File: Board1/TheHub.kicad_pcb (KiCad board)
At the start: 2 copper layers, 195.6 x 195.6 mm, 56 parts, among them J1 ARM_ADC_1, J10 SCIENCE + WHEELS POWER CONN, J11 RFD900, J12 I2C_1 Test Point, J13 I2C_2 Test Point, J14 ARDUINO NANO LEFT, J15 GPIO Test, J16 I2C_3 Test Point, J17 12V OUT, J18 7.4V IN, J19 ANALOG SENSORS, J2 ARM_ADC_2, J20 GPS, J21 COMPASS, J22 ARDUINO NANO RIGHT, J23 NucleoRight, J3 ARM_PWM_OUT, J4 ARM POWER CONN, J5 NucleoLeft, J6 SCI_ADC_1, J7 SCIENCE_PWM_OUT, J8 12V MAIN POWER, J9 WHEEL_ADC_1, U1 PRE-PCA9685, U2 PRE-ADS1115, U3 PRE-ADS1115, U4 PRE-PCA9685, U5 PRE-ADS1115, U6 TL1963, U7 LM340MP-5.0, U9 PRE-ADS1115

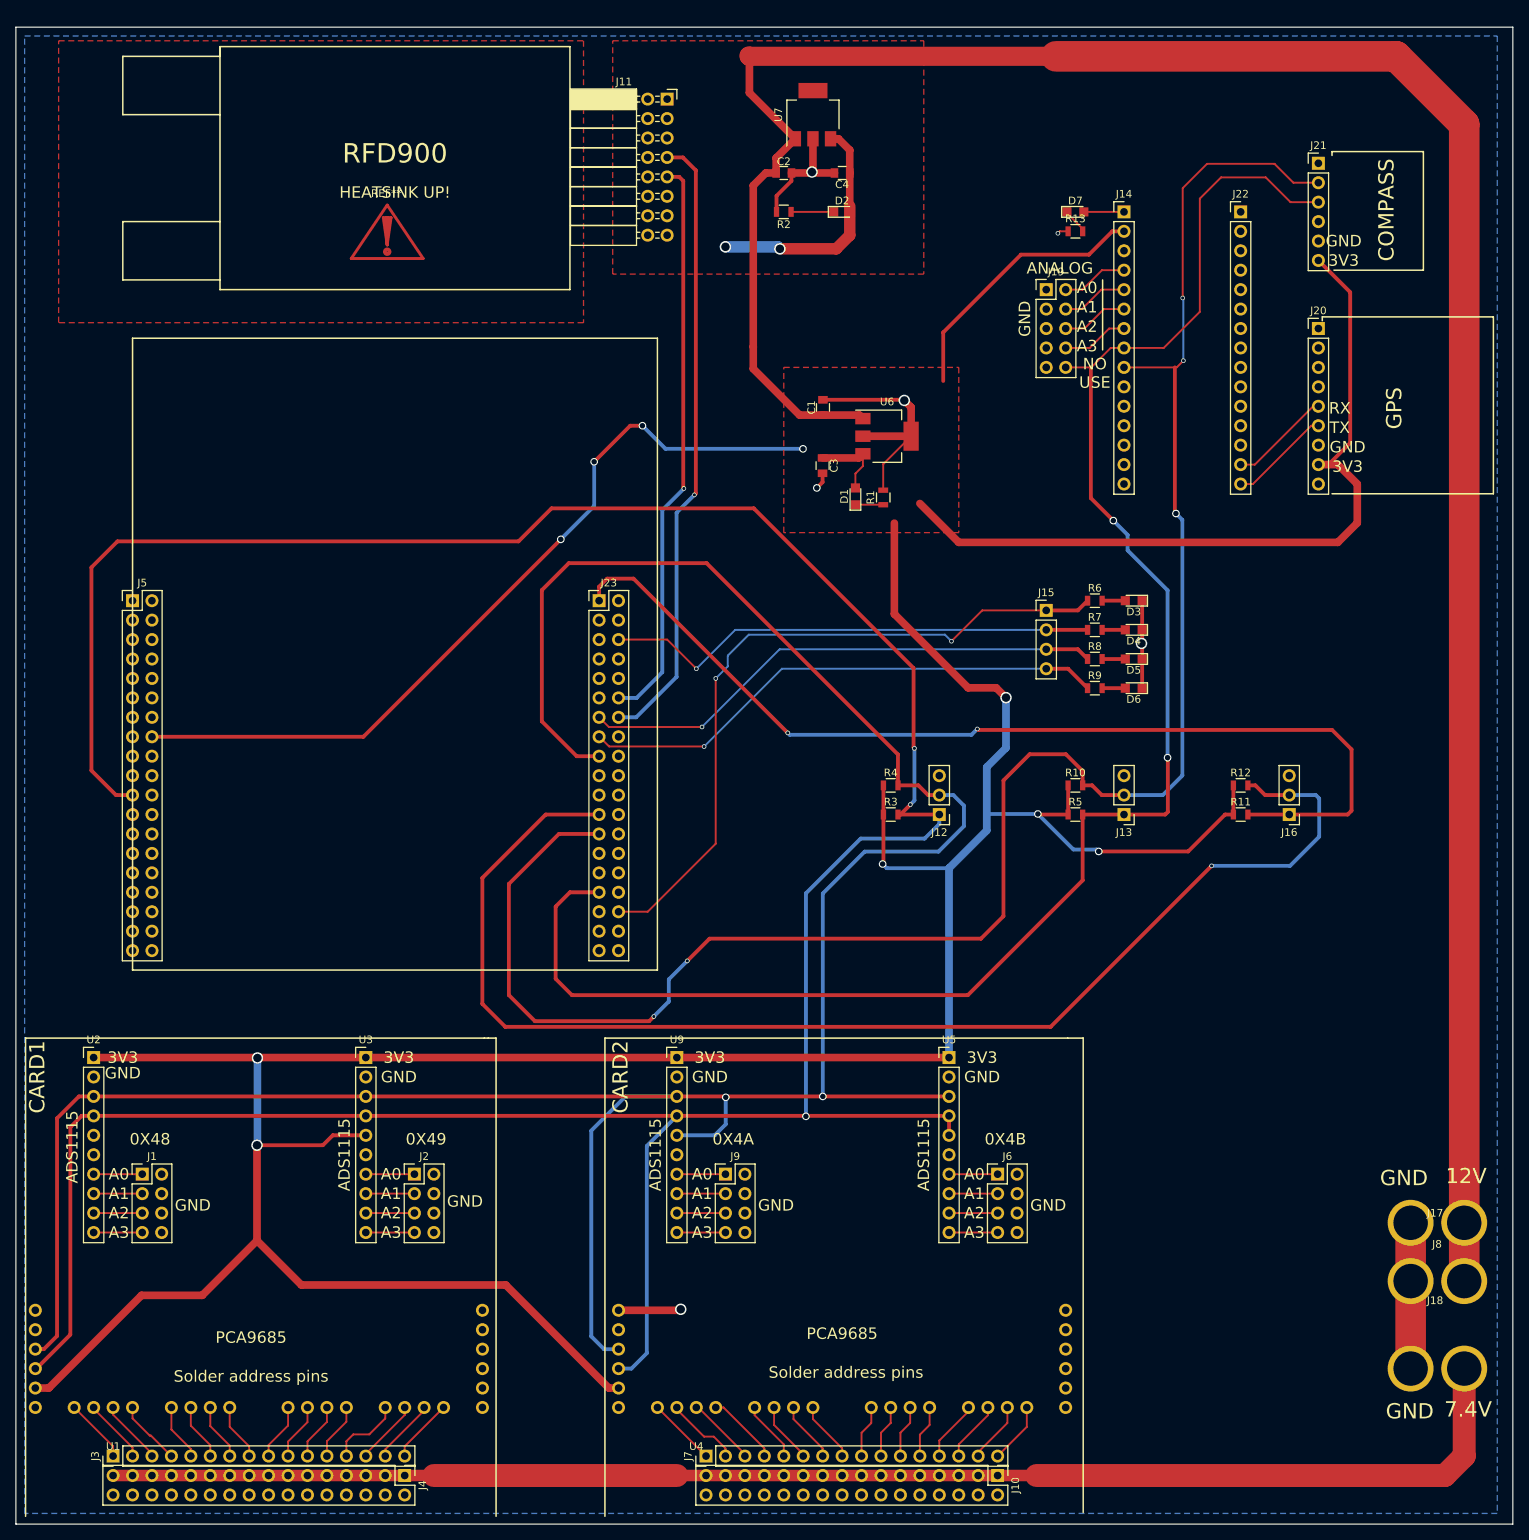
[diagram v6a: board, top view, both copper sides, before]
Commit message: Add M3 Mouting Holes
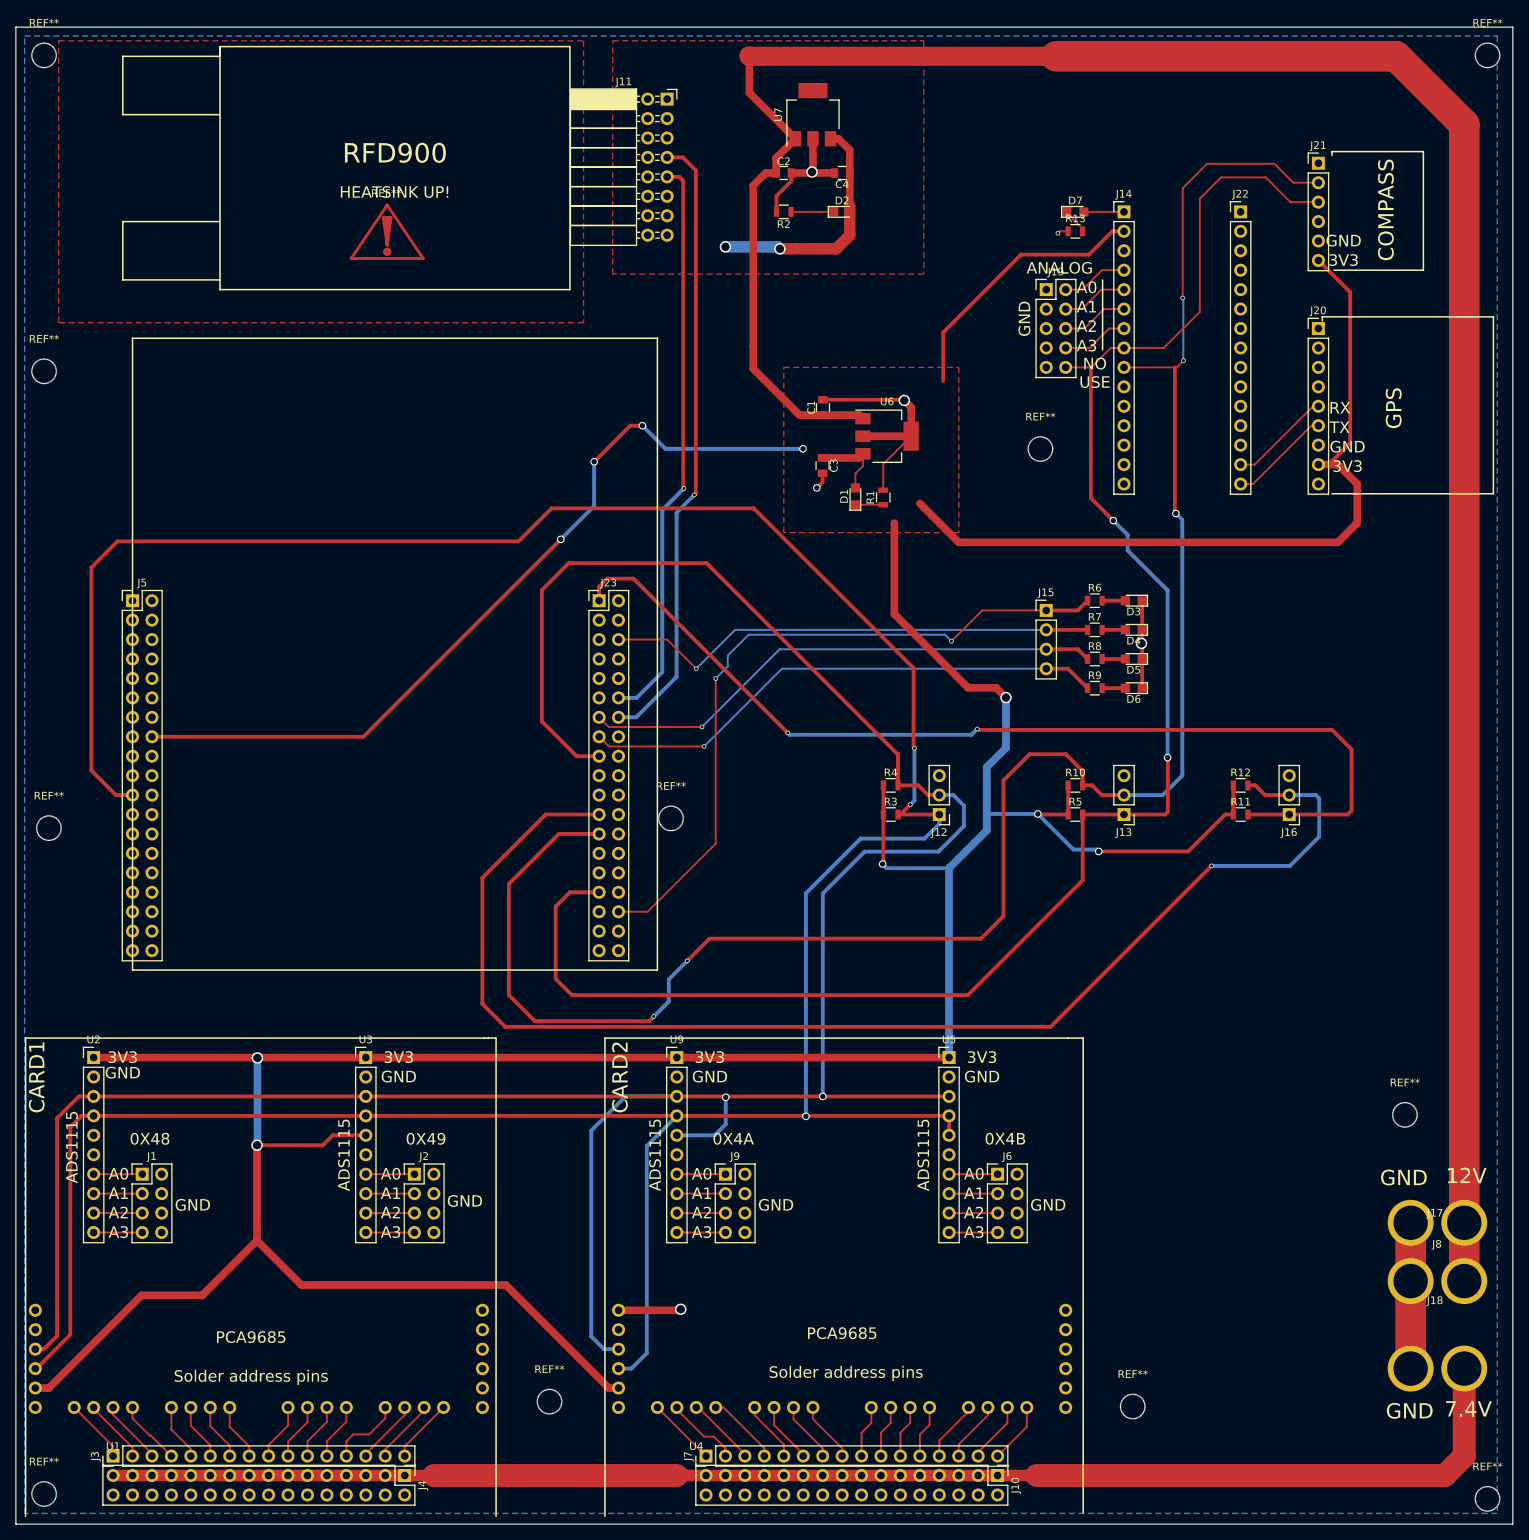
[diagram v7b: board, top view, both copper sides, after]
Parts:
- added REF**: MountingHole_3.2mm_M3, Mounting_Holes:MountingHole_3.2mm_M3, F.Cu at (131.4, 229.9)
- added REF**: MountingHole_3.2mm_M3, Mounting_Holes:MountingHole_3.2mm_M3, F.Cu at (243.2, 192.4)
- added REF**: MountingHole_3.2mm_M3, Mounting_Holes:MountingHole_3.2mm_M3, F.Cu at (207.6, 230.5)
- added REF**: MountingHole_3.2mm_M3, Mounting_Holes:MountingHole_3.2mm_M3, F.Cu at (254.0, 242.6)
- added REF**: MountingHole_3.2mm_M3, Mounting_Holes:MountingHole_3.2mm_M3, F.Cu at (254.0, 54.0)
- added REF**: MountingHole_3.2mm_M3, Mounting_Holes:MountingHole_3.2mm_M3, F.Cu at (65.4, 54.0)
- added REF**: MountingHole_3.2mm_M3, Mounting_Holes:MountingHole_3.2mm_M3, F.Cu at (65.4, 95.2)
- added REF**: MountingHole_3.2mm_M3, Mounting_Holes:MountingHole_3.2mm_M3, F.Cu at (65.4, 241.9)
- added REF**: MountingHole_3.2mm_M3, Mounting_Holes:MountingHole_3.2mm_M3, F.Cu at (66.0, 154.9)
- added REF**: MountingHole_3.2mm_M3, Mounting_Holes:MountingHole_3.2mm_M3, F.Cu at (147.3, 153.7)
- added REF**: MountingHole_3.2mm_M3, Mounting_Holes:MountingHole_3.2mm_M3, F.Cu at (195.6, 105.4)
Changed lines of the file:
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@@
     (tracks 577)
     (zones 0)
-    (modules 56)
+    (modules 67)
     (nets 179)
   )
@@
     (fp_line (start -0.508 -2.54) (end 0 -2.54) (layer F.Cu) (width 0.381))
   )
+  (module Mounting_Holes:MountingHole_3.2mm_M3 (layer F.Cu)
+    (at 254 242.57)
+    (descr "Mounting Hole 3.2mm, no annular, M3")
+    (tags "mounting hole 3.2mm no annular m3")
+    (fp_text reference REF** (at 0 -4.2) (layer F.SilkS)
+      (effects (font (size 1 1) (thickness 0.15)))
+    )
+    (fp_text value MountingHole_3.2mm_M3 (at 0 4.2) (layer F.Fab)
+      (effects (font (size 1 1) (thickness 0.15)))
+    )
+    (fp_circle (center 0 0) (end 3.2 0) (layer Cmts.User) (width 0.15))
+    (fp_circle (center 0 0) (end 3.45 0) (layer F.CrtYd) (width 0.05))
+    (pad 1 np_thru_hole circle (at 0 0) (size 3.2 3.2) (drill 3.2) (layers *.Cu *.Mask))
+  )
+  (module Mounting_Holes:MountingHole_3.2mm_M3 (layer F.Cu)
+    (at 254 53.975)
+    (descr "Mounting Hole 3.2mm, no annular, M3")
+    (tags "mounting hole 3.2mm no annular m3")
+    (fp_text reference REF** (at 0 -4.2) (layer F.SilkS)
+      (effects (font (size 1 1) (thickness 0.15)))
+    )
+    (fp_text value MountingHole_3.2mm_M3 (at 0 4.2) (layer F.Fab)
+      (effects (font (size 1 1) (thickness 0.15)))
+    )
+    (fp_circle (center 0 0) (end 3.2 0) (layer Cmts.User) (width 0.15))
+    (fp_circle (center 0 0) (end 3.45 0) (layer F.CrtYd) (width 0.05))
+    (pad 1 np_thru_hole circle (at 0 0) (size 3.2 3.2) (drill 3.2) (layers *.Cu *.Mask))
+  )
+  (module Mounting_Holes:MountingHole_3.2mm_M3 (layer F.Cu)
+    (at 65.405 53.975)
+    (descr "Mounting Hole 3.2mm, no annular, M3")
+    (tags "mounting hole 3.2mm no annular m3")
+    (fp_text reference REF** (at 0 -4.2) (layer F.SilkS)
+      (effects (font (size 1 1) (thickness 0.15)))
+    )
+    (fp_text value MountingHole_3.2mm_M3 (at 0 4.2) (layer F.Fab)
+      (effects (font (size 1 1) (thickness 0.15)))
+    )
+    (fp_circle (center 0 0) (end 3.2 0) (layer Cmts.User) (width 0.15))
+    (fp_circle (center 0 0) (end 3.45 0) (layer F.CrtYd) (width 0.05))
+    (pad 1 np_thru_hole circle (at 0 0) (size 3.2 3.2) (drill 3.2) (layers *.Cu *.Mask))
+  )
+  (module Mounting_Holes:MountingHole_3.2mm_M3 (layer F.Cu)
+    (at 65.405 95.25)
+    (descr "Mounting Hole 3.2mm, no annular, M3")
+    (tags "mounting hole 3.2mm no annular m3")
+    (fp_text reference REF** (at 0 -4.2) (layer F.SilkS)
+      (effects (font (size 1 1) (thickness 0.15)))
+    )
+    (fp_text value MountingHole_3.2mm_M3 (at 0 4.2) (layer F.Fab)
+      (effects (font (size 1 1) (thickness 0.15)))
+    )
+    (fp_circle (center 0 0) (end 3.2 0) (layer Cmts.User) (width 0.15))
+    (fp_circle (center 0 0) (end 3.45 0) (layer F.CrtYd) (width 0.05))
+    (pad 1 np_thru_hole circle (at 0 0) (size 3.2 3.2) (drill 3.2) (layers *.Cu *.Mask))
+  )
+  (module Mounting_Holes:MountingHole_3.2mm_M3 (layer F.Cu)
+    (at 65.405 241.935)
+    (descr "Mounting Hole 3.2mm, no annular, M3")
+    (tags "mounting hole 3.2mm no annular m3")
+    (fp_text reference REF** (at 0 -4.2) (layer F.SilkS)
+      (effects (font (size 1 1) (thickness 0.15)))
+    )
+    (fp_text value MountingHole_3.2mm_M3 (at 0 4.2) (layer F.Fab)
+      (effects (font (size 1 1) (thickness 0.15)))
+    )
+    (fp_circle (center 0 0) (end 3.2 0) (layer Cmts.User) (width 0.15))
+    (fp_circle (center 0 0) (end 3.45 0) (layer F.CrtYd) (width 0.05))
+    (pad 1 np_thru_hole circle (at 0 0) (size 3.2 3.2) (drill 3.2) (layers *.Cu *.Mask))
+  )
+  (module Mounting_Holes:MountingHole_3.2mm_M3 (layer F.Cu)
+    (at 66.04 154.94)
+    (descr "Mounting Hole 3.2mm, no annular, M3")
+    (tags "mounting hole 3.2mm no annular m3")
+    (fp_text reference REF** (at 0 -4.2) (layer F.SilkS)
+      (effects (font (size 1 1) (thickness 0.15)))
+    )
+    (fp_text value MountingHole_3.2mm_M3 (at 0 4.2) (layer F.Fab)
+      (effects (font (size 1 1) (thickness 0.15)))
+    )
+    (fp_circle (center 0 0) (end 3.2 0) (layer Cmts.User) (width 0.15))
+    (fp_circle (center 0 0) (end 3.45 0) (layer F.CrtYd) (width 0.05))
+    (pad 1 np_thru_hole circle (at 0 0) (size 3.2 3.2) (drill 3.2) (layers *.Cu *.Mask))
+  )
+  (module Mounting_Holes:MountingHole_3.2mm_M3 (layer F.Cu)
+    (at 147.32 153.67)
+    (descr "Mounting Hole 3.2mm, no annular, M3")
+    (tags "mounting hole 3.2mm no annular m3")
+    (fp_text reference REF** (at 0 -4.2) (layer F.SilkS)
+      (effects (font (size 1 1) (thickness 0.15)))
+    )
+    (fp_text value MountingHole_3.2mm_M3 (at 0 4.2) (layer F.Fab)
+      (effects (font (size 1 1) (thickness 0.15)))
+    )
+    (fp_circle (center 0 0) (end 3.2 0) (layer Cmts.User) (width 0.15))
+    (fp_circle (center 0 0) (end 3.45 0) (layer F.CrtYd) (width 0.05))
+    (pad 1 np_thru_hole circle (at 0 0) (size 3.2 3.2) (drill 3.2) (layers *.Cu *.Mask))
+  )
+  (module Mounting_Holes:MountingHole_3.2mm_M3 (layer F.Cu)
+    (at 195.58 105.41)
+    (descr "Mounting Hole 3.2mm, no annular, M3")
+    (tags "mounting hole 3.2mm no annular m3")
+    (fp_text reference REF** (at 0 -4.2) (layer F.SilkS)
+      (effects (font (size 1 1) (thickness 0.15)))
+    )
+    (fp_text value MountingHole_3.2mm_M3 (at 0 4.2) (layer F.Fab)
+      (effects (font (size 1 1) (thickness 0.15)))
+    )
+    (fp_circle (center 0 0) (end 3.2 0) (layer Cmts.User) (width 0.15))
+    (fp_circle (center 0 0) (end 3.45 0) (layer F.CrtYd) (width 0.05))
+    (pad 1 np_thru_hole circle (at 0 0) (size 3.2 3.2) (drill 3.2) (layers *.Cu *.Mask))
+  )
+  (module Mounting_Holes:MountingHole_3.2mm_M3 (layer F.Cu)
+    (at 131.445 229.87)
+    (descr "Mounting Hole 3.2mm, no annular, M3")
+    (tags "mounting hole 3.2mm no annular m3")
+    (fp_text reference REF** (at 0 -4.2) (layer F.SilkS)
+      (effects (font (size 1 1) (thickness 0.15)))
+    )
+    (fp_text value MountingHole_3.2mm_M3 (at 0 4.2) (layer F.Fab)
+      (effects (font (size 1 1) (thickness 0.15)))
+    )
+    (fp_circle (center 0 0) (end 3.2 0) (layer Cmts.User) (width 0.15))
+    (fp_circle (center 0 0) (end 3.45 0) (layer F.CrtYd) (width 0.05))
+    (pad 1 np_thru_hole circle (at 0 0) (size 3.2 3.2) (drill 3.2) (layers *.Cu *.Mask))
+  )
+  (module Mounting_Holes:MountingHole_3.2mm_M3 (layer F.Cu)
+    (at 243.205 192.405)
+    (descr "Mounting Hole 3.2mm, no annular, M3")
+    (tags "mounting hole 3.2mm no annular m3")
+    (fp_text reference REF** (at 0 -4.2) (layer F.SilkS)
+      (effects (font (size 1 1) (thickness 0.15)))
+    )
+    (fp_text value MountingHole_3.2mm_M3 (at 0 4.2) (layer F.Fab)
+      (effects (font (size 1 1) (thickness 0.15)))
+    )
+    (fp_circle (center 0 0) (end 3.2 0) (layer Cmts.User) (width 0.15))
+    (fp_circle (center 0 0) (end 3.45 0) (layer F.CrtYd) (width 0.05))
+    (pad 1 np_thru_hole circle (at 0 0) (size 3.2 3.2) (drill 3.2) (layers *.Cu *.Mask))
+  )
+  (module Mounting_Holes:MountingHole_3.2mm_M3 (layer F.Cu)
+    (at 207.645 230.505)
+    (descr "Mounting Hole 3.2mm, no annular, M3")
+    (tags "mounting hole 3.2mm no annular m3")
+    (fp_text reference REF** (at 0 -4.2) (layer F.SilkS)
+      (effects (font (size 1 1) (thickness 0.15)))
+    )
+    (fp_text value MountingHole_3.2mm_M3 (at 0 4.2) (layer F.Fab)
+      (effects (font (size 1 1) (thickness 0.15)))
+    )
+    (fp_circle (center 0 0) (end 3.2 0) (layer Cmts.User) (width 0.15))
+    (fp_circle (center 0 0) (end 3.45 0) (layer F.CrtYd) (width 0.05))
+    (pad 1 np_thru_hole circle (at 0 0) (size 3.2 3.2) (drill 3.2) (layers *.Cu *.Mask))
+  )
   (gr_text GND (at 235.204 78.232) (layer F.SilkS)
